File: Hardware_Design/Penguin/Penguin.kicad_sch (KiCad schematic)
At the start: 15 parts, among them SW1 SW_Push, U1 STM32F405RGT6

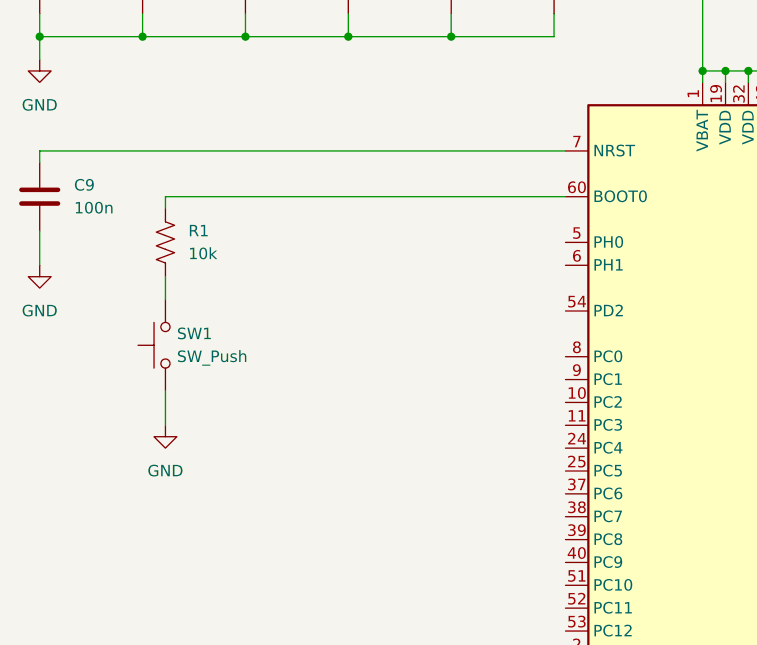
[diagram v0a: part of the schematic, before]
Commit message: Updated switch to dual pole to prevent floating values on boot
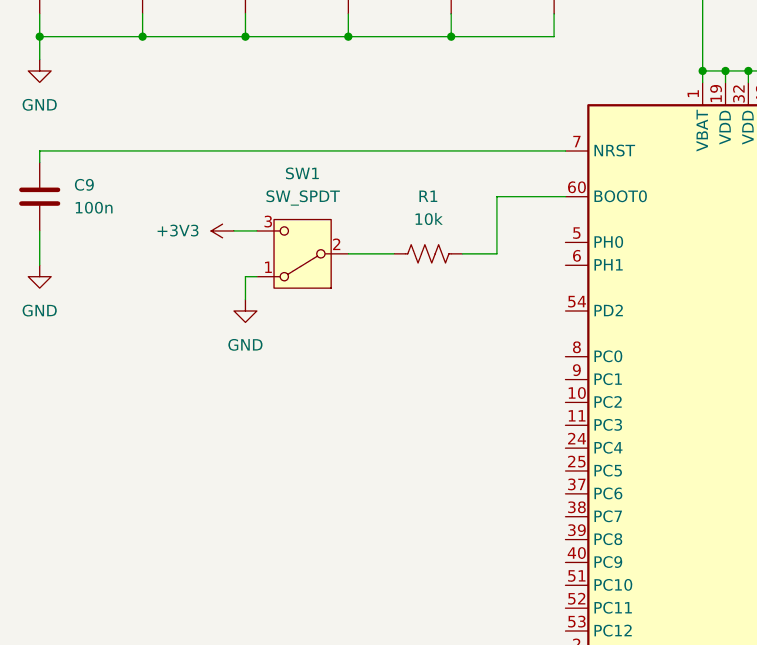
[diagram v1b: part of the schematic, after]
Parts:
- removed SW1: SW_Push, symbol Switch:SW_Push
- added SW1: SW_SPDT, symbol Switch:SW_SPDT
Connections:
- net +3V3: now also SW1.3 (C)
- net GND: now also SW1.1 (A)
- net at R1.1: now also U1.60 (BOOT0)
- net at R1.2: now also SW1.2 (B); no longer U1.60 (BOOT0)
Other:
- moved on the sheet: R1
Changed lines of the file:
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@@
-	(wire
-		(pts
-			(xy 128.27 55.88) (xy 83.82 55.88)
-		)
-		(stroke
-			(width 0)
-			(type default)
-		)
-	)
 	(wire
 		(pts
@@
 	(wire
 		(pts
+			(xy 92.71 64.77) (xy 93.98 64.77)
+		)
+		(stroke
+			(width 0)
+			(type default)
+		)
+	)
+	(wire
+		(pts
 			(xy 148.59 139.7) (xy 148.59 142.24)
 		)
@@
 	(wire
 		(pts
+			(xy 91.44 59.69) (xy 93.98 59.69)
+		)
+		(stroke
+			(width 0)
+			(type default)
+		)
+	)
+	(wire
+		(pts
 			(xy 146.05 41.91) (xy 148.59 41.91)
 		)
@@
 	(wire
 		(pts
-			(xy 83.82 77.47) (xy 83.82 81.28)
-		)
-		(stroke
-			(width 0)
-			(type default)
-		)
-	)
-	(wire
-		(pts
 			(xy 156.21 43.18) (xy 156.21 25.4)
 		)
@@
 	(wire
 		(pts
+			(xy 104.14 62.23) (xy 109.22 62.23)
+		)
+		(stroke
+			(width 0)
+			(type default)
+		)
+	)
+	(wire
+		(pts
 			(xy 128.27 116.84) (xy 105.41 116.84)
 		)
@@
 	(wire
 		(pts
-			(xy 83.82 64.77) (xy 83.82 67.31)
-		)
-		(stroke
-			(width 0)
-			(type default)
-		)
-	)
-	(wire
-		(pts
 			(xy 128.27 119.38) (xy 118.11 119.38)
 		)
@@
 	(wire
 		(pts
+			(xy 120.65 62.23) (xy 120.65 55.88)
+		)
+		(stroke
+			(width 0)
+			(type default)
+		)
+	)
+	(wire
+		(pts
 			(xy 115.57 25.4) (xy 115.57 27.94)
 		)
@@
 	(wire
 		(pts
+			(xy 120.65 55.88) (xy 128.27 55.88)
+		)
+		(stroke
+			(width 0)
+			(type default)
+		)
+	)
+	(wire
+		(pts
 			(xy 176.53 25.4) (xy 187.96 25.4)
 		)
@@
 	(wire
 		(pts
-			(xy 83.82 55.88) (xy 83.82 57.15)
-		)
-		(stroke
-			(width 0)
-			(type default)
-		)
-	)
-	(wire
-		(pts
 			(xy 187.96 35.56) (xy 187.96 38.1)
 		)
@@
 	(wire
 		(pts
+			(xy 92.71 64.77) (xy 92.71 67.31)
+		)
+		(stroke
+			(width 0)
+			(type default)
+		)
+	)
+	(wire
+		(pts
 			(xy 187.96 38.1) (xy 187.96 40.64)
+		)
+		(stroke
+			(width 0)
+			(type default)
+		)
+	)
+	(wire
+		(pts
+			(xy 116.84 62.23) (xy 120.65 62.23)
 		)
 		(stroke
@@
 	(symbol
 		(lib_id "Device:R_US")
-		(at 83.82 60.96 180)
+		(at 113.03 62.23 270)
 		(unit 1)
 		(exclude_from_sim no)
@@
 		(fields_autoplaced yes)
 		(property "Reference" "R1"
-			(at 86.36 59.6899 0)
-			(effects
-				(font
-					(size 1.27 1.27)
-				)
-				(justify right)
+			(at 113.03 55.88 90)
+			(effects
+				(font
+					(size 1.27 1.27)
+				)
 			)
 		)
 		(property "Value" "10k"
-			(at 86.36 62.2299 0)
-			(effects
-				(font
-					(size 1.27 1.27)
-				)
-				(justify right)
+			(at 113.03 58.42 90)
+			(effects
+				(font
+					(size 1.27 1.27)
+				)
 			)
 		)
 		(property "Footprint" ""
-			(at 82.804 60.706 90)
+			(at 112.776 63.246 90)
 			(effects
 				(font
@@
 		)
 		(property "Datasheet" "~"
-			(at 83.82 60.96 0)
+			(at 113.03 62.23 0)
 			(effects
 				(font
@@
 		)
 		(property "Description" "Resistor, US symbol"
-			(at 83.82 60.96 0)
+			(at 113.03 62.23 0)
 			(effects
 				(font
@@
 	)
 	(symbol
+		(lib_id "power:+3V3")
+		(at 91.44 59.69 90)
+		(unit 1)
+		(exclude_from_sim no)
+		(in_bom yes)
+		(on_board yes)
+		(dnp no)
+		(fields_autoplaced yes)
+		(property "Reference" "#PWR011"
+			(at 95.25 59.69 0)
+			(effects
+				(font
+					(size 1.27 1.27)
+				)
+				(hide yes)
+			)
+		)
+		(property "Value" "+3V3"
+			(at 87.63 59.6899 90)
+			(effects
+				(font
+					(size 1.27 1.27)
+				)
+				(justify left)
+			)
+		)
+		(property "Footprint" ""
+			(at 91.44 59.69 0)
+			(effects
+				(font
+					(size 1.27 1.27)
+				)
+				(hide yes)
+			)
+		)
+		(property "Datasheet" ""
+			(at 91.44 59.69 0)
+			(effects
+				(font
+					(size 1.27 1.27)
+				)
+				(hide yes)
+			)
+		)
+		(property "Description" "Power symbol creates a global label with name \"+3V3\""
+			(at 91.44 59.69 0)
+			(effects
+				(font
+					(size 1.27 1.27)
+				)
+				(hide yes)
+			)
+		)
+		(pin "1"
+		)
+		(instances
+			(project "Penguin"
+				(path "/f071372f-a84c-461d-8a40-4a0ade99ed6d"
+					(reference "#PWR011")
+					(unit 1)
+				)
+			)
+		)
+	)
+	(symbol
 		(lib_id "Device:C")
 		(at 127 31.75 0)
@@
 	(symbol
 		(lib_id "power:GND")
-		(at 83.82 81.28 0)
+		(at 92.71 67.31 0)
 		(unit 1)
 		(exclude_from_sim no)
@@
 		(fields_autoplaced yes)
 		(property "Reference" "#PWR010"
-			(at 83.82 87.63 0)
+			(at 92.71 73.66 0)
 			(effects
 				(font
@@
 		)
 		(property "Value" "GND"
-			(at 83.82 86.36 0)
+			(at 92.71 72.39 0)
 			(effects
 				(font
@@
 		)
 		(property "Footprint" ""
-			(at 83.82 81.28 0)
+			(at 92.71 67.31 0)
 			(effects
 				(font
@@
 		)
 		(property "Datasheet" ""
-			(at 83.82 81.28 0)
+			(at 92.71 67.31 0)
 			(effects
 				(font
@@
 		)
 		(property "Description" "Power symbol creates a global label with name \"GND\" , ground"
-			(at 83.82 81.28 0)
+			(at 92.71 67.31 0)
 			(effects
 				(font
@@
 				(path "/f071372f-a84c-461d-8a40-4a0ade99ed6d"
 					(reference "#PWR010")
+					(unit 1)
+				)
+			)
+		)
+	)
+	(symbol
+		(lib_id "Switch:SW_SPDT")
+		(at 99.06 62.23 180)
+		(unit 1)
+		(exclude_from_sim no)
+		(in_bom yes)
+		(on_board yes)
+		(dnp no)
+		(fields_autoplaced yes)
+		(property "Reference" "SW1"
+			(at 99.06 53.34 0)
+			(effects
+				(font
+					(size 1.27 1.27)
+				)
+			)
+		)
+		(property "Value" "SW_SPDT"
+			(at 99.06 55.88 0)
+			(effects
+				(font
+					(size 1.27 1.27)
+				)
+			)
+		)
+		(property "Footprint" ""
+			(at 99.06 62.23 0)
+			(effects
+				(font
+					(size 1.27 1.27)
+				)
+				(hide yes)
+			)
+		)
+		(property "Datasheet" "~"
+			(at 99.06 54.61 0)
+			(effects
+				(font
+					(size 1.27 1.27)
+				)
+				(hide yes)
+			)
+		)
+		(property "Description" "Switch, single pole double throw"
+			(at 99.06 62.23 0)
+			(effects
+				(font
+					(size 1.27 1.27)
+				)
+				(hide yes)
+			)
+		)
+		(pin "3"
+		)
+		(pin "1"
+		)
+		(pin "2"
+		)
+		(instances
+			(project ""
+				(path "/f071372f-a84c-461d-8a40-4a0ade99ed6d"
+					(reference "SW1")
 					(unit 1)
 				)
@@
 					(unit 1)
 				)
-			)
-		)
-	)
-	(symbol
-		(lib_id "Switch:SW_Push")
-		(at 83.82 72.39 90)
-		(unit 1)
-		(exclude_from_sim no)
-		(in_bom yes)
-		(on_board yes)
-		(dnp no)
-		(fields_autoplaced yes)
-		(property "Reference" "SW1"
-			(at 85.09 71.1199 90)
-			(effects
-				(font
-					(size 1.27 1.27)
-				)
-				(justify right)
-			)
-		)
-		(property "Value" "SW_Push"
-			(at 85.09 73.6599 90)
-			(effects
-				(font
-					(size 1.27 1.27)
-				)
-				(justify right)
-			)
-		)
-		(property "Footprint" ""
-			(at 78.74 72.39 0)
-			(effects
-				(font
-					(size 1.27 1.27)
-				)
-				(hide yes)
-			)
-		)
-		(property "Datasheet" "~"
-			(at 78.74 72.39 0)
-			(effects
-				(font
-					(size 1.27 1.27)
-				)
-				(hide yes)
-			)
-		)
-		(property "Description" "Push button switch, generic, two pins"
-			(at 83.82 72.39 0)
-			(effects
-				(font
-					(size 1.27 1.27)
-				)
-				(hide yes)
-			)
-		)
-		(pin "1"
-		)
-		(pin "2"
-		)
-		(instances
-			(project ""
-				(path "/f071372f-a84c-461d-8a40-4a0ade99ed6d"
-					(reference "SW1")
-					(unit 1)
-				)
